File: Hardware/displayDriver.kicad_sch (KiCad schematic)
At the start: 10 parts, among them U6 4511, U7 HDSP-816E, U8 4511, U9 HDSP-816E

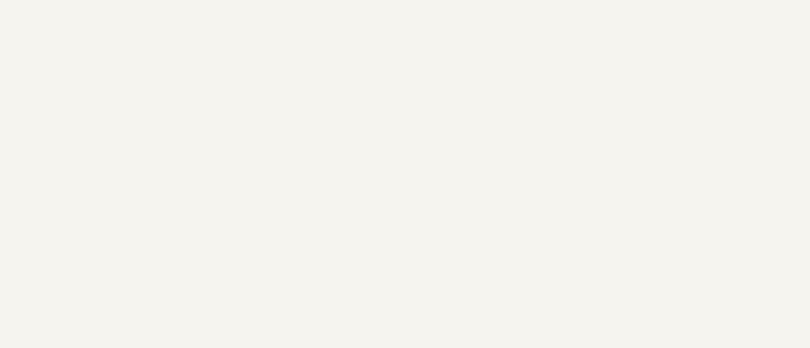
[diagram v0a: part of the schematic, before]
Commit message: Add in BCD net-labels and clean up drawings.
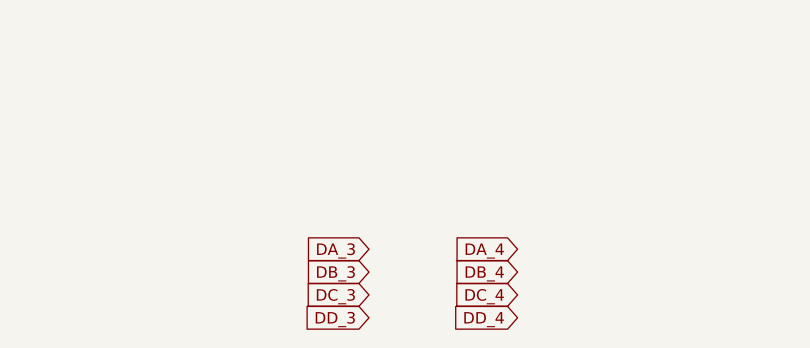
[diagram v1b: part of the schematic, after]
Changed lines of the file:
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@@
+		)
+	)
+	(global_label "DD_4"
+		(shape input)
+		(at 144.78 114.3 180)
+		(effects
+			(font
+				(size 1.27 1.27)
+			)
+			(justify right)
+		)
+		(property "Intersheetrefs" "${INTERSHEET_REFS}"
+			(at 144.78 114.3 0)
+			(effects
+				(font
+					(size 1.27 1.27)
+				)
+				(hide yes)
+			)
+		)
+	)
+	(global_label "DB_4"
+		(shape input)
+		(at 144.78 109.22 180)
+		(effects
+			(font
+				(size 1.27 1.27)
+			)
+			(justify right)
+		)
+		(property "Intersheetrefs" "${INTERSHEET_REFS}"
+			(at 144.78 109.22 0)
+			(effects
+				(font
+					(size 1.27 1.27)
+				)
+				(hide yes)
+			)
+		)
+	)
+	(global_label "DC_3"
+		(shape input)
+		(at 128.27 111.76 180)
+		(effects
+			(font
+				(size 1.27 1.27)
+			)
+			(justify right)
+		)
+		(property "Intersheetrefs" "${INTERSHEET_REFS}"
+			(at 128.27 111.76 0)
+			(effects
+				(font
+					(size 1.27 1.27)
+				)
+				(hide yes)
+			)
 		)
 	)
@@
 		)
 	)
+	(global_label "DA_3"
+		(shape input)
+		(at 128.27 106.68 180)
+		(effects
+			(font
+				(size 1.27 1.27)
+			)
+			(justify right)
+		)
+		(property "Intersheetrefs" "${INTERSHEET_REFS}"
+			(at 128.27 106.68 0)
+			(effects
+				(font
+					(size 1.27 1.27)
+				)
+				(hide yes)
+			)
+		)
+	)
+	(global_label "DA_4"
+		(shape input)
+		(at 144.78 106.68 180)
+		(effects
+			(font
+				(size 1.27 1.27)
+			)
+			(justify right)
+		)
+		(property "Intersheetrefs" "${INTERSHEET_REFS}"
+			(at 144.78 106.68 0)
+			(effects
+				(font
+					(size 1.27 1.27)
+				)
+				(hide yes)
+			)
+		)
+	)
+	(global_label "DD_3"
+		(shape input)
+		(at 128.27 114.3 180)
+		(effects
+			(font
+				(size 1.27 1.27)
+			)
+			(justify right)
+		)
+		(property "Intersheetrefs" "${INTERSHEET_REFS}"
+			(at 128.27 114.3 0)
+			(effects
+				(font
+					(size 1.27 1.27)
+				)
+				(hide yes)
+			)
+		)
+	)
 	(global_label "DC_1"
 		(shape input)
@@
 		)
 	)
+	(global_label "DB_3"
+		(shape input)
+		(at 128.27 109.22 180)
+		(effects
+			(font
+				(size 1.27 1.27)
+			)
+			(justify right)
+		)
+		(property "Intersheetrefs" "${INTERSHEET_REFS}"
+			(at 128.27 109.22 0)
+			(effects
+				(font
+					(size 1.27 1.27)
+				)
+				(hide yes)
+			)
+		)
+	)
 	(global_label "DD_1"
 		(shape input)
@@
 			(effects
 				(font
+					(size 1.27 1.27)
+				)
+				(hide yes)
+			)
+		)
+	)
+	(global_label "DC_4"
+		(shape input)
+		(at 144.78 111.76 180)
+		(effects
+			(font
+				(size 1.27 1.27)
+			)
+			(justify right)
+		)
+		(property "Intersheetrefs" "${INTERSHEET_REFS}"
+			(at 144.78 111.76 0)
+			(effects
+				(font

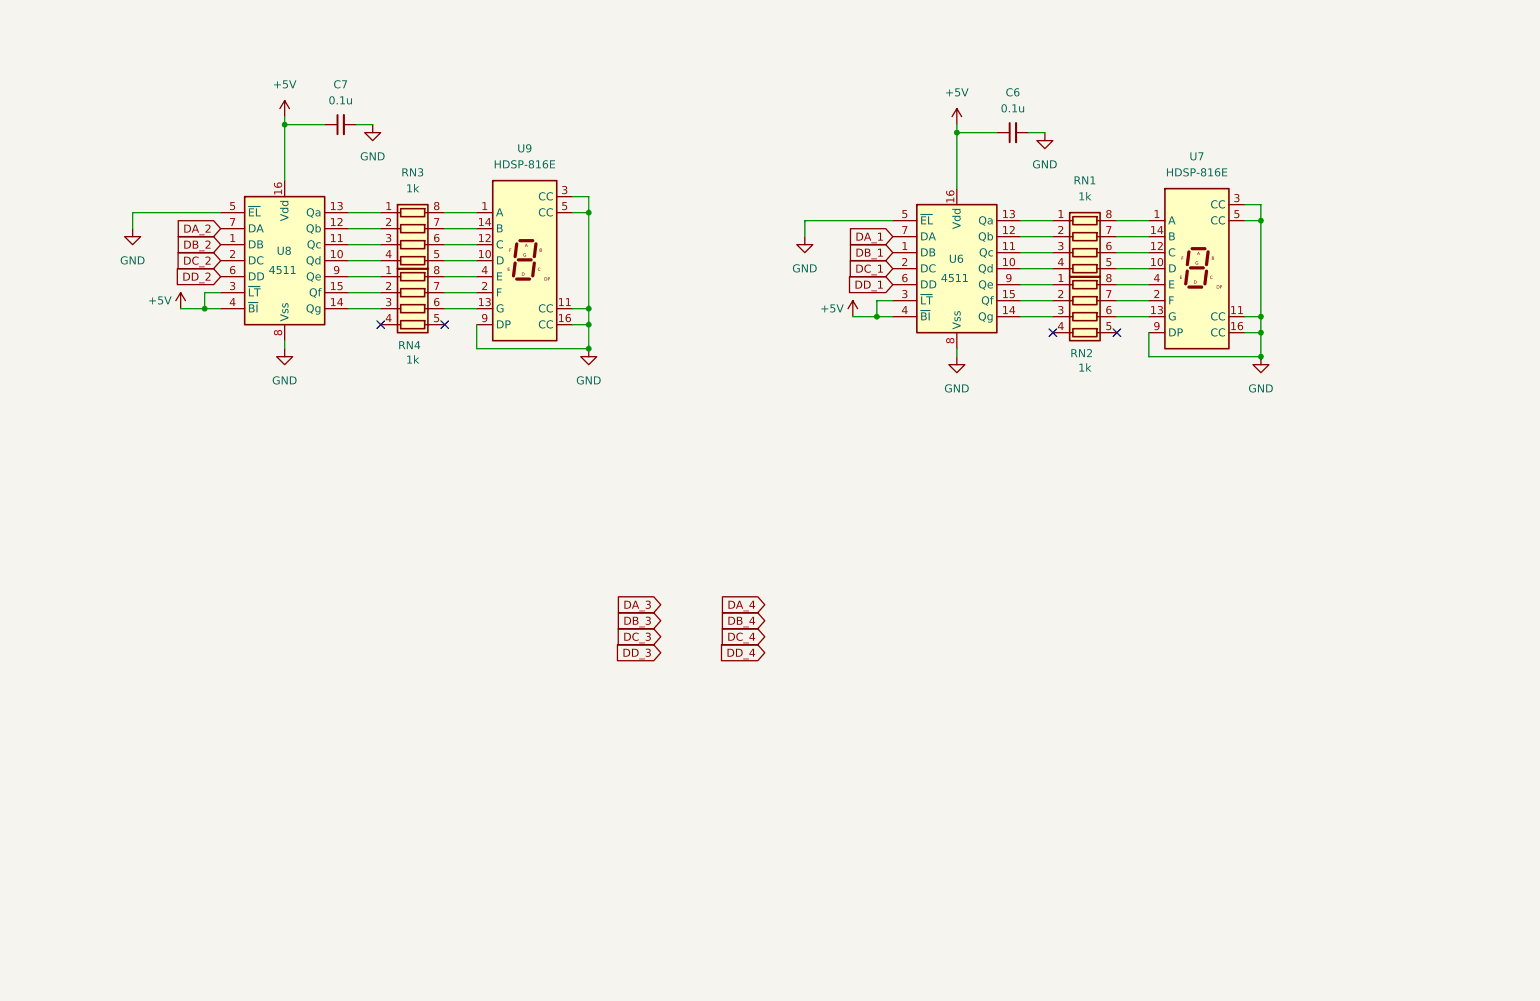
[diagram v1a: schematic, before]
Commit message: Add in hours and 10-hour display driver
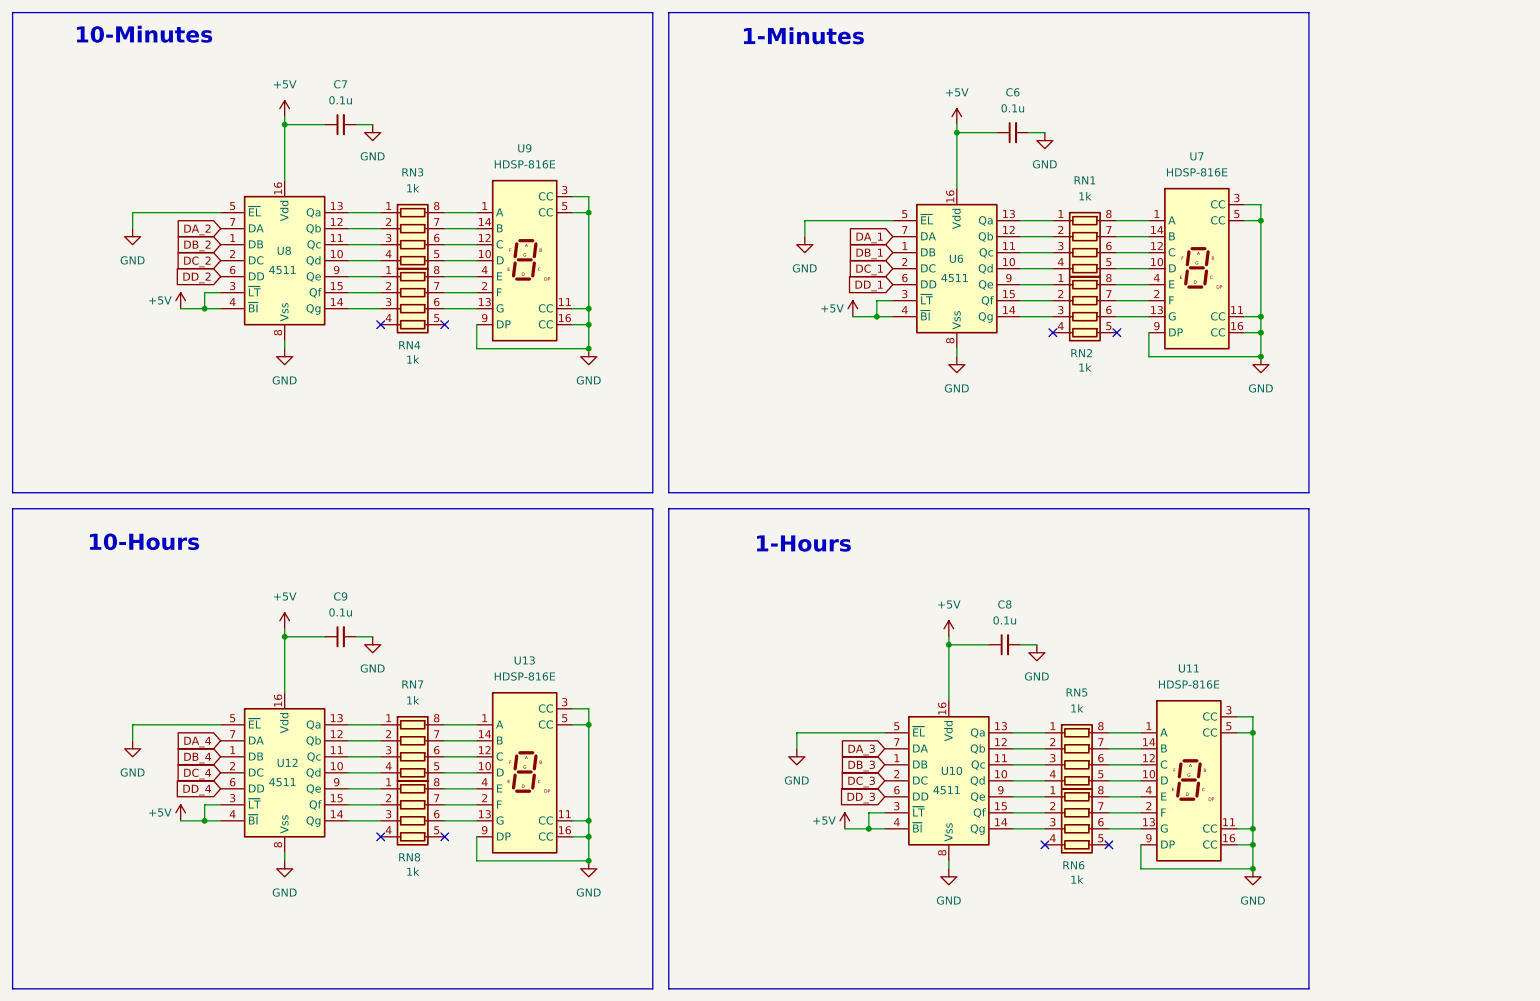
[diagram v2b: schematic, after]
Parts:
- added C8, C9: 0.1u, symbol Device:C_Small
- added RN5, RN6, RN7, RN8: 1k, symbol Device:R_Pack04
- added U10, U12: 4511, symbol 4xxx_IEEE:4511
- added U11, U13: HDSP-816E, symbol JKC_library:HDSP-816E
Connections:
- net +5V: now also C8.1, C9.1, U10.16 (Vdd), U10.3 (~{LT}), U10.4 (~{BI}), U12.16 (Vdd), U12.3 (~{LT}), U12.4 (~{BI})
- net DA_3: now also U10.7 (DA)
- net DA_4: now also U12.7 (DA)
- net DB_3: now also U10.1 (DB)
- net DB_4: now also U12.1 (DB)
- net DC_3: now also U10.2 (DC)
- net DC_4: now also U12.2 (DC)
- net DD_3: now also U10.6 (DD)
- net DD_4: now also U12.6 (DD)
- net GND: now also C8.2, C9.2, U10.5 (~{EL}), U10.8 (Vss), U11.11 (CC), U11.16 (CC), U11.3 (CC), U11.5 (CC), U11.9 (DP), U12.5 (~{EL}), U12.8 (Vss), U13.11 (CC), U13.16 (CC), U13.3 (CC), U13.5 (CC), U13.9 (DP)
- new net: RN7.1 (R1.1), U12.13 (Qa)
- new net: RN7.2 (R2.1), U12.12 (Qb)
- new net: RN7.3 (R3.1), U12.11 (Qc)
- new net: RN7.4 (R4.1), U12.10 (Qd)
- new net: RN7.5 (R4.2), U13.10 (D)
- new net: RN7.6 (R3.2), U13.12 (C)
- new net: RN7.7 (R2.2), U13.14 (B)
- new net: RN7.8 (R1.2), U13.1 (A)
- new net: RN8.6 (R3.2), U13.13 (G)
- new net: RN8.7 (R2.2), U13.2 (F)
- new net: RN8.8 (R1.2), U13.4 (E)
- new net: RN8.1 (R1.1), U12.9 (Qe)
- new net: RN8.2 (R2.1), U12.15 (Qf)
- new net: RN8.3 (R3.1), U12.14 (Qg)
- new net: RN6.1 (R1.1), U10.9 (Qe)
- new net: RN6.2 (R2.1), U10.15 (Qf)
- new net: RN6.3 (R3.1), U10.14 (Qg)
- new net: RN6.6 (R3.2), U11.13 (G)
- new net: RN6.7 (R2.2), U11.2 (F)
- new net: RN6.8 (R1.2), U11.4 (E)
- new net: RN5.8 (R1.2), U11.1 (A)
- new net: RN5.5 (R4.2), U11.10 (D)
- new net: RN5.6 (R3.2), U11.12 (C)
- new net: RN5.7 (R2.2), U11.14 (B)
- new net: RN5.1 (R1.1), U10.13 (Qa)
- new net: RN5.2 (R2.1), U10.12 (Qb)
- new net: RN5.3 (R3.1), U10.11 (Qc)
- new net: RN5.4 (R4.1), U10.10 (Qd)
- no-connect marks 4 -> 8
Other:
- note added: "1-Hours"
- note added: "1-Minutes"
- note added: "10-Hours"
- note added: "10-Minutes"

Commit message: Add pushbuttons to be able to set time
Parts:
- U11, U13, U7, U9: footprint (none) -> JKC_Library:Broadcom_HDSP-81x
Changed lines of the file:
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@@
 			)
 		)
-		(property "Footprint" ""
+		(property "Footprint" "JKC_Library:Broadcom_HDSP-81x"
 			(at 106.68 133.35 0)
 			(effects
@@
 			)
 		)
-		(property "Footprint" ""
+		(property "Footprint" "JKC_Library:Broadcom_HDSP-81x"
 			(at 213.36 53.34 0)
 			(effects
@@
 			)
 		)
-		(property "Footprint" ""
+		(property "Footprint" "JKC_Library:Broadcom_HDSP-81x"
 			(at 106.68 52.07 0)
 			(effects
@@
 			)
 		)
-		(property "Footprint" ""
+		(property "Footprint" "JKC_Library:Broadcom_HDSP-81x"
 			(at 212.09 134.62 0)
 			(effects

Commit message: Set Footprints for components
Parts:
- C6, C7, C8, C9: footprint (none) -> Capacitor_SMD:C_0603_1608Metric
- RN1, RN2, RN3, RN4, RN5, RN6, RN7, RN8: footprint (none) -> Resistor_SMD:R_Array_Convex_4x0603
- U10, U12, U6, U8: footprint (none) -> Package_SO:TSSOP-16_4.4x5mm_P0.65mm
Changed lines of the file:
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@@
 			)
 		)
-		(property "Footprint" ""
+		(property "Footprint" "Resistor_SMD:R_Array_Convex_4x0603"
 			(at 88.9 137.795 90)
 			(effects
@@
 			)
 		)
-		(property "Footprint" ""
+		(property "Footprint" "Resistor_SMD:R_Array_Convex_4x0603"
 			(at 195.58 67.945 90)
 			(effects
@@
 			)
 		)
-		(property "Footprint" ""
+		(property "Footprint" "Resistor_SMD:R_Array_Convex_4x0603"
 			(at 88.9 147.955 90)
 			(effects
@@
 			)
 		)
-		(property "Footprint" ""
+		(property "Footprint" "Capacitor_SMD:C_0603_1608Metric"
 			(at 77.47 111.76 0)
 			(effects
@@
 			)
 		)
-		(property "Footprint" ""
+		(property "Footprint" "Package_SO:TSSOP-16_4.4x5mm_P0.65mm"
 			(at 175.26 53.34 0)
 			(effects
@@
 			)
 		)
-		(property "Footprint" ""
+		(property "Footprint" "Capacitor_SMD:C_0603_1608Metric"
 			(at 77.47 30.48 0)
 			(effects
@@
 			)
 		)
-		(property "Footprint" ""
+		(property "Footprint" "Resistor_SMD:R_Array_Convex_4x0603"
 			(at 88.9 66.675 90)
 			(effects
@@
 			)
 		)
-		(property "Footprint" ""
+		(property "Footprint" "Package_SO:TSSOP-16_4.4x5mm_P0.65mm"
 			(at 68.58 52.07 0)
 			(effects
@@
 			)
 		)
-		(property "Footprint" ""
+		(property "Footprint" "Capacitor_SMD:C_0603_1608Metric"
 			(at 184.15 31.75 0)
 			(effects
@@
 			)
 		)
-		(property "Footprint" ""
+		(property "Footprint" "Resistor_SMD:R_Array_Convex_4x0603"
 			(at 195.58 57.785 90)
 			(effects
@@
 			)
 		)
-		(property "Footprint" ""
+		(property "Footprint" "Capacitor_SMD:C_0603_1608Metric"
 			(at 182.88 113.03 0)
 			(effects
@@
 			)
 		)
-		(property "Footprint" ""
+		(property "Footprint" "Resistor_SMD:R_Array_Convex_4x0603"
 			(at 194.31 149.225 90)
 			(effects
@@
 			)
 		)
-		(property "Footprint" ""
+		(property "Footprint" "Resistor_SMD:R_Array_Convex_4x0603"
 			(at 194.31 139.065 90)
 			(effects
@@
 			)
 		)
-		(property "Footprint" ""
+		(property "Footprint" "Resistor_SMD:R_Array_Convex_4x0603"
 			(at 88.9 56.515 90)
 			(effects
@@
 			)
 		)
-		(property "Footprint" ""
+		(property "Footprint" "Package_SO:TSSOP-16_4.4x5mm_P0.65mm"
 			(at 68.58 133.35 0)
 			(effects
@@
 			)
 		)
-		(property "Footprint" ""
+		(property "Footprint" "Package_SO:TSSOP-16_4.4x5mm_P0.65mm"
 			(at 173.99 134.62 0)
 			(effects

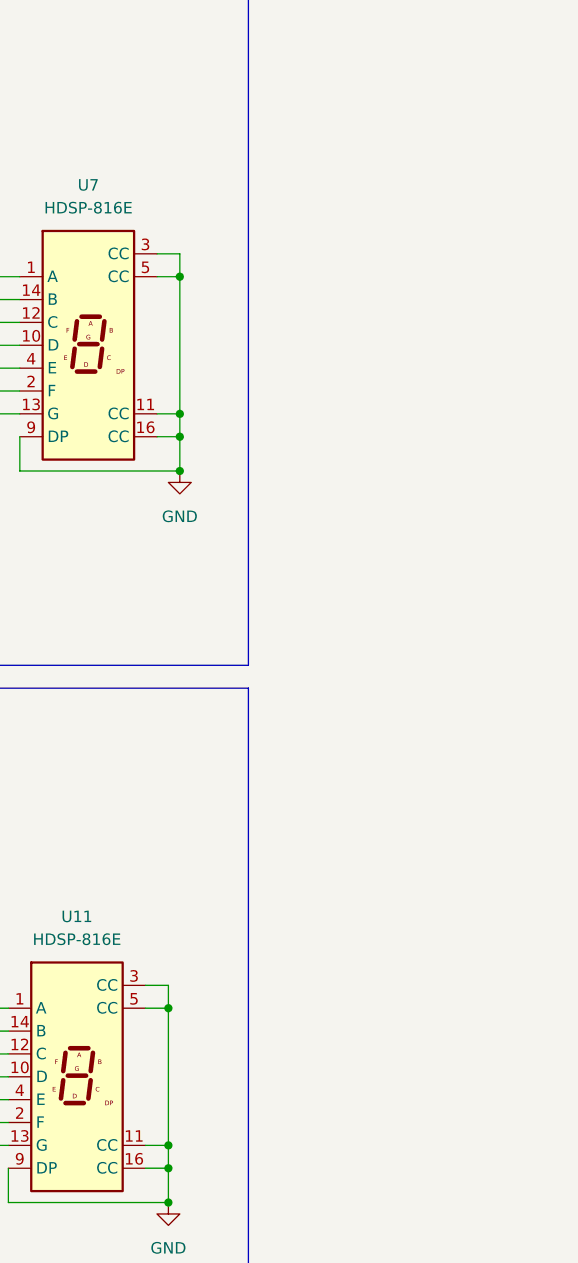
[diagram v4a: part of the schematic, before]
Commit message: Add in connectors for display board interconnect
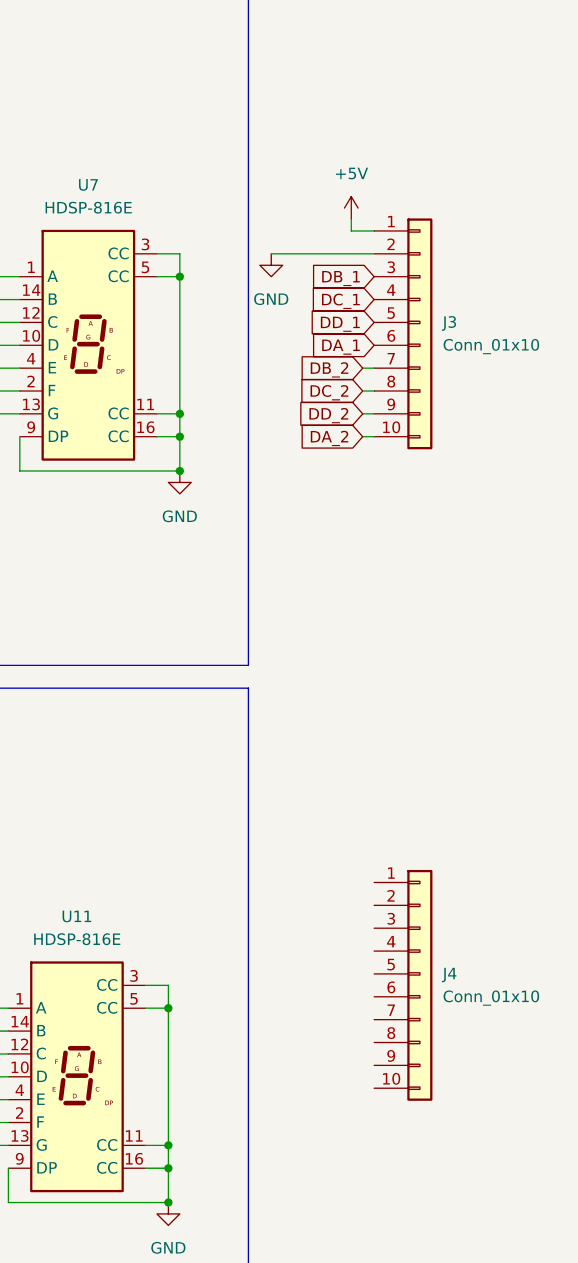
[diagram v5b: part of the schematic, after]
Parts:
- added J3, J4: Conn_01x10, Connector_PinHeader_2.54mm:PinHeader_1x10_P2.54mm_Vertical, symbol Connector_Generic:Conn_01x10
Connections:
- net +5V: now also J3.1 (Pin_1)
- net DA_1: now also J3.6 (Pin_6)
- net DA_2: now also J3.10 (Pin_10)
- net DB_1: now also J3.3 (Pin_3)
- net DB_2: now also J3.7 (Pin_7)
- net DC_1: now also J3.4 (Pin_4)
- net DC_2: now also J3.8 (Pin_8)
- net DD_1: now also J3.5 (Pin_5)
- net DD_2: now also J3.9 (Pin_9)
- net GND: now also J3.2 (Pin_2)
